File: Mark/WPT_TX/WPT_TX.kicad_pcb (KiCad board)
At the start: 2 copper layers, 113 parts, among them J1 Conn_01x01, J10 Conn_01x01, J2 Conn_01x01, J3 Conn_Coaxial, J4 Conn_Coaxial, J5 Conn_Coaxial, J6 Conn_02x05_Odd_Even, J7 Conn_01x03, J8 Conn_01x04, J9 Conn_01x01, Q1 NMOS, Q2 NMOS, Q3 NMOS, Q4 NMOS, U1 INA240A1D, U10 LM5106, U11 MCP2515-QFN20, U12 MCP2562-E-MF, U13 LM5106, U2 LM2937IMP-3.3, U3 LM2936-5.0, U4 LM2937IMP-12, U5 LMC6032, U6 CD4043BDR, U7 BTS6142DAUMA1, U8 SN74LVC1G14DBV, U9 ATSAMD21G16B-MFT, Y1 32.7680kHz, Y2 8MHz

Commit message: Added input caps
- Forgot input capacitors, oops
- Updated sim based on cap selection, achieving 87% efficiency, low loss on caps!
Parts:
- added C35: 330u, Capacitor_SMD:CP_Elec_10x12.5, F.Cu at (97.1, 56.9)
- added C36: 330u, Capacitor_SMD:CP_Elec_10x12.5, F.Cu at (111.7, 44.9)
- added C37: 330u, Capacitor_SMD:CP_Elec_10x12.5, F.Cu at (111.7, 56.9)
- added C38: 330u, Capacitor_SMD:CP_Elec_10x12.5, F.Cu at (126.2, 44.9)
- moved C10 80.5 mm to (42.7, 80.9)
- moved C11 80.5 mm to (42.7, 85.6)
- moved C13 80.5 mm to (61.4, 69.9)
- moved C16 80.5 mm to (50.4, 80.8)
- moved C17 80.5 mm to (52.6, 72.7)
- moved C18 80.5 mm to (56.5, 72.7)
- moved C19 80.5 mm to (46.6, 85.6)
- moved C2 80.5 mm to (46.6, 80.9)
- moved C20 80.5 mm to (55.8, 77.4)
- moved C22 80.5 mm to (50.4, 83.2)
- moved C23 80.5 mm to (65.3, 69.9)
- moved C24 80.5 mm to (145.8, 85.8)
- moved C25 80.5 mm to (60.3, 74.6)
- moved C30 80.5 mm to (136.0, 95.5)
- moved C31 80.5 mm to (54.3, 80.1)
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
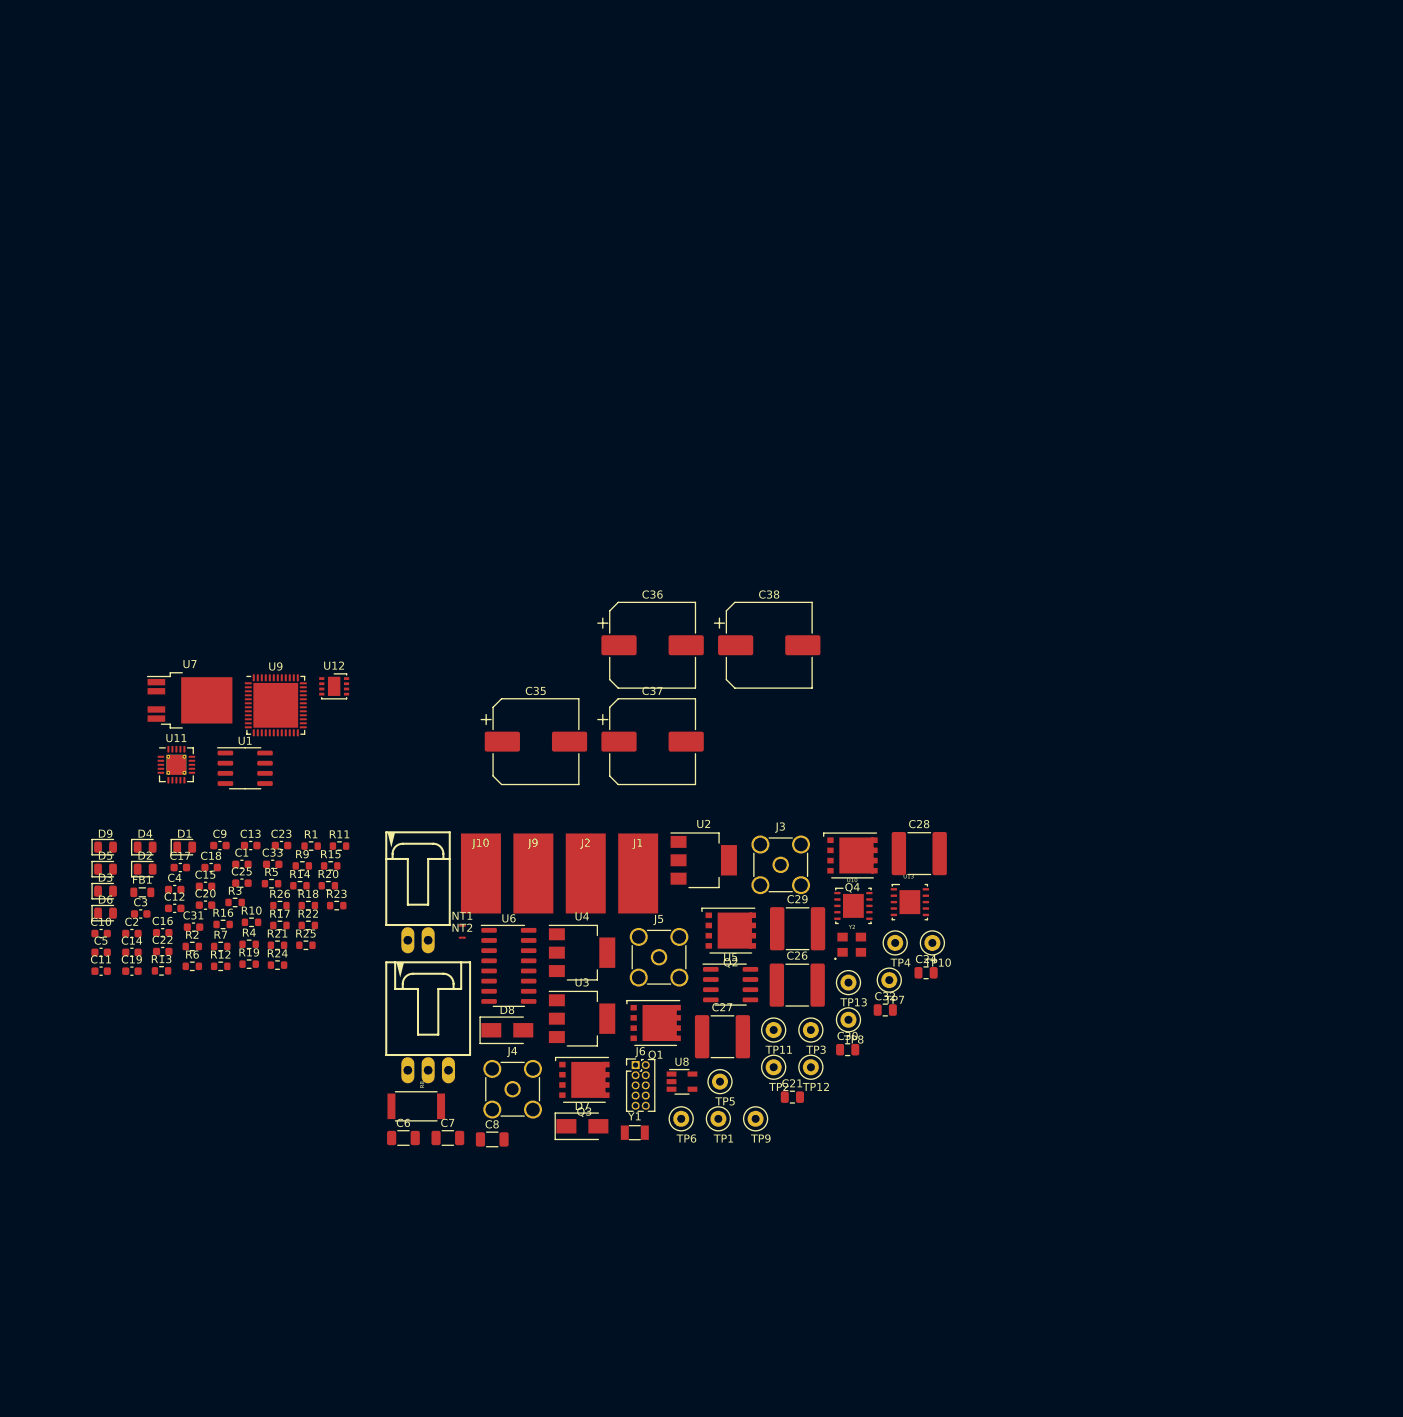
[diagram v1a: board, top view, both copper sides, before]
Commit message: Initial Layout
- Started on layout, board shape.
- Probably will need to get a little larger, but its pretty good
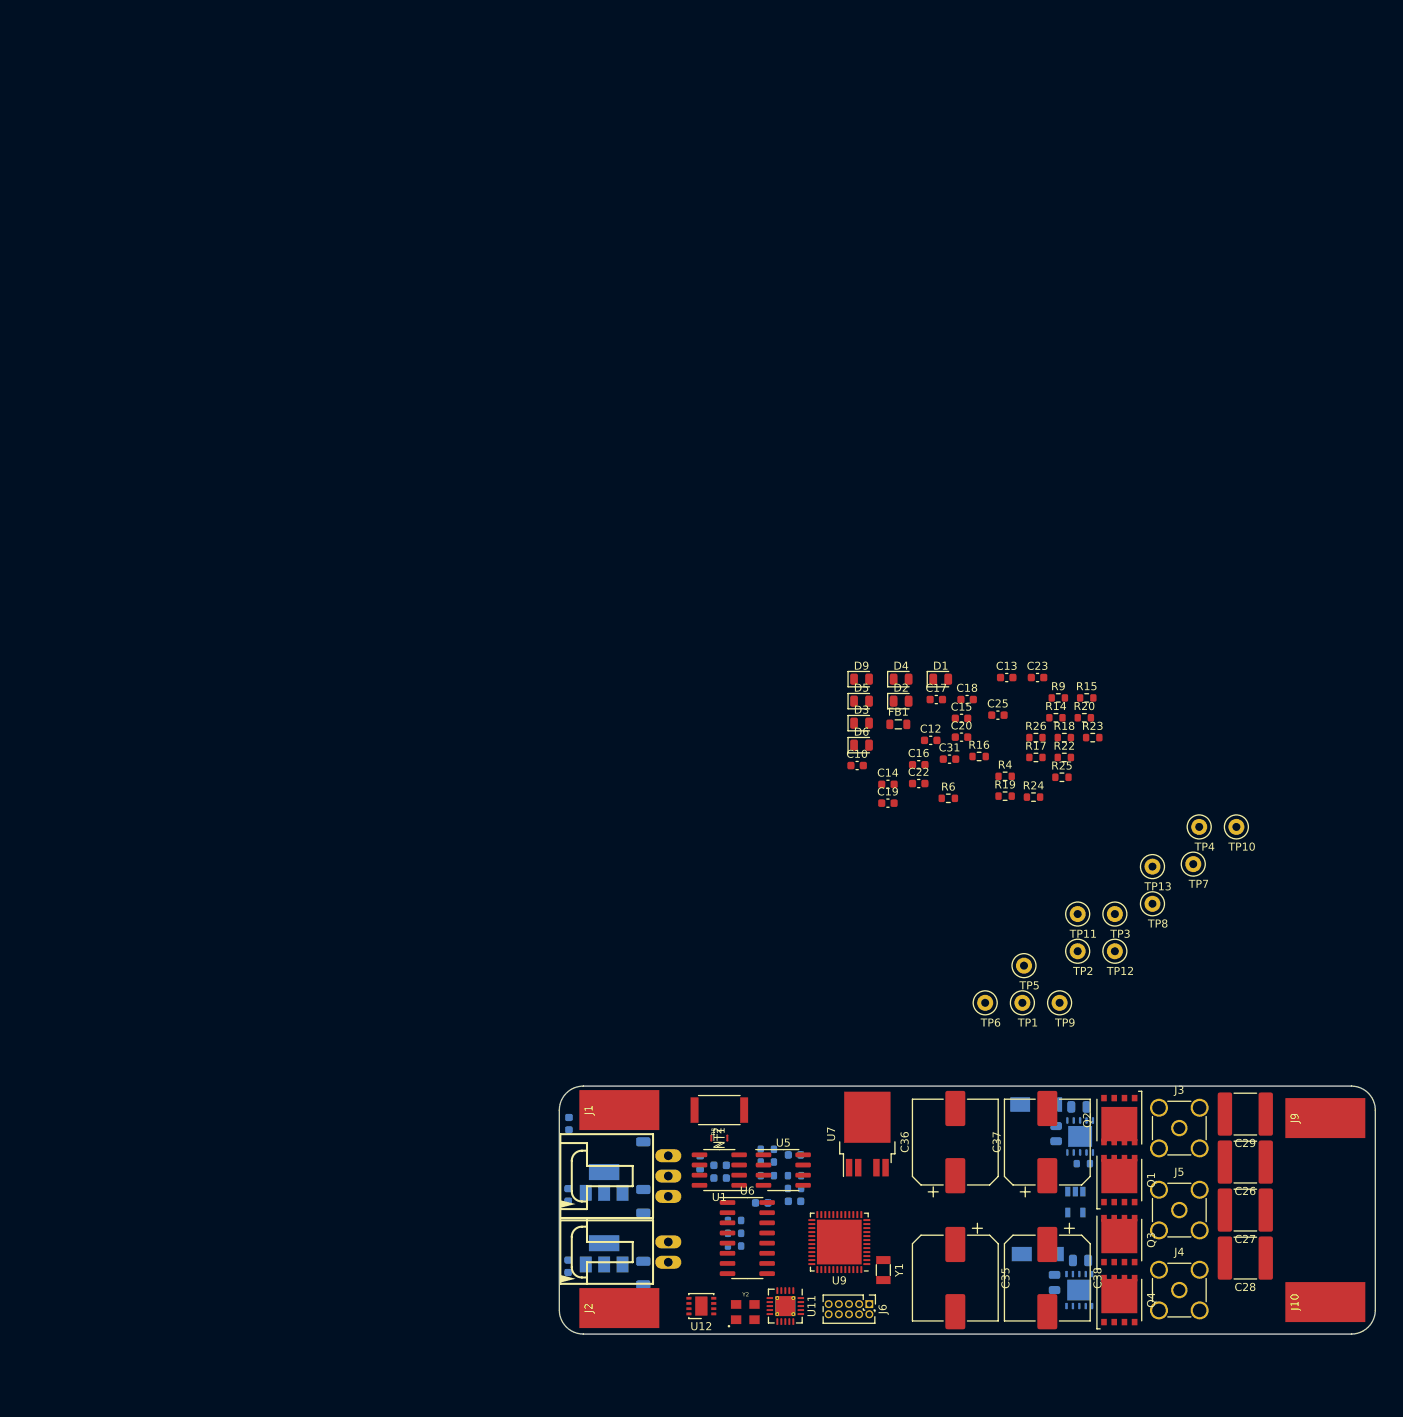
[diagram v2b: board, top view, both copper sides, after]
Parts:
- C1, C11, C2, C21, C24, C3, C30, C32, C33, C4, C5, C6, C7, C8, C9, D7, D8, R1, R10, R11, R12, R13, R2, R21, R3, R5, R7, U10, U13, U2, U3, U4, U8: moved to B.Cu
- moved J10 118.4 mm to (195.8, 127.0), turned to 90 degrees
- moved R21 104.4 mm to (165.5, 109.7)
- moved J9 103.6 mm to (195.8, 104.0), turned to 90 degrees
- moved U11 101.8 mm to (128.2, 127.5), turned to 270 degrees
- moved U7 100.5 mm to (138.5, 106.0), turned to 90 degrees
- moved U9 97.3 mm to (135.0, 119.5), turned to 180 degrees
- moved R15 96.8 mm to (165.9, 51.5)
- moved R23 96.8 mm to (166.7, 56.4)
- moved C10 96.8 mm to (137.2, 59.9)
- moved C12 96.8 mm to (146.4, 56.8)
- moved C13 96.8 mm to (155.9, 48.9)
- moved C15 96.8 mm to (150.3, 54.0)
- moved C16 96.8 mm to (144.9, 59.8)
- moved C17 96.8 mm to (147.1, 51.7)
- moved C18 96.8 mm to (151.0, 51.7)
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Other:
- board outline added: 102 x 31 mm
- copper layers 2 -> 4

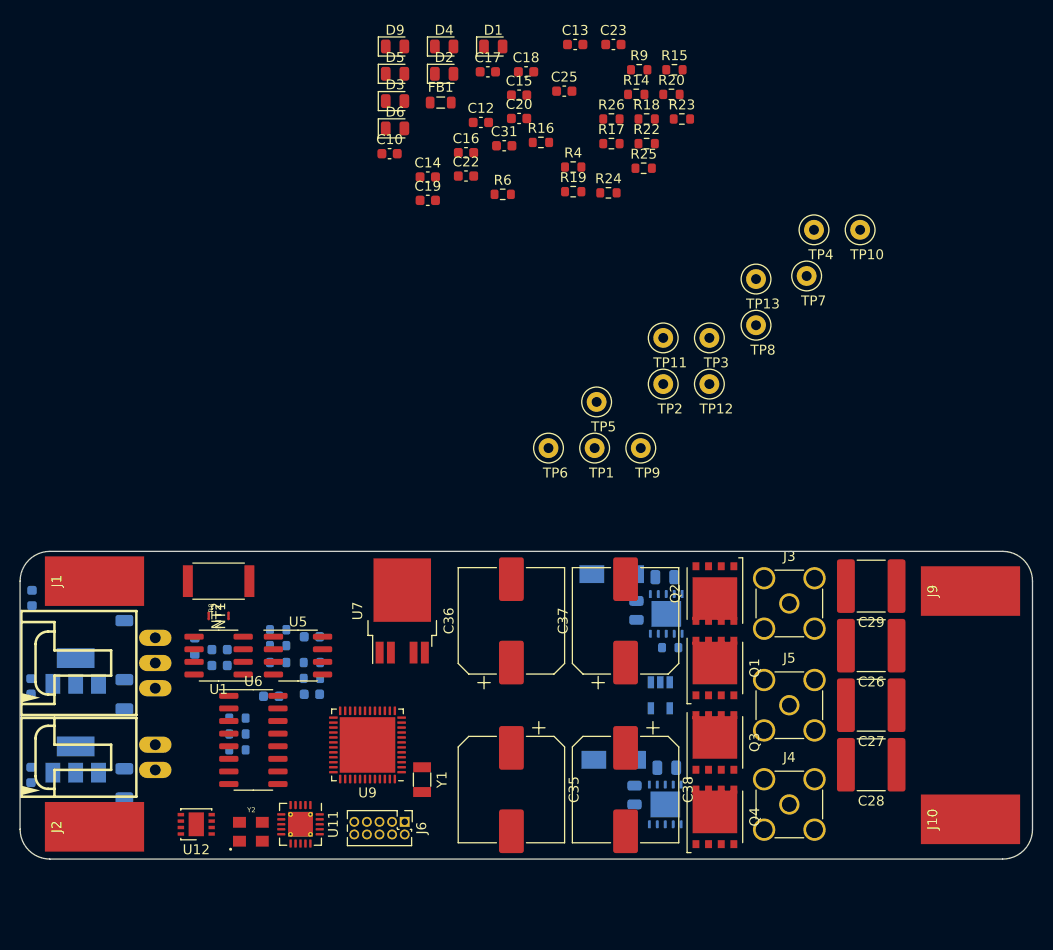
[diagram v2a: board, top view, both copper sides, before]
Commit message: Layout
- Finished expected layout. Going for routing next.
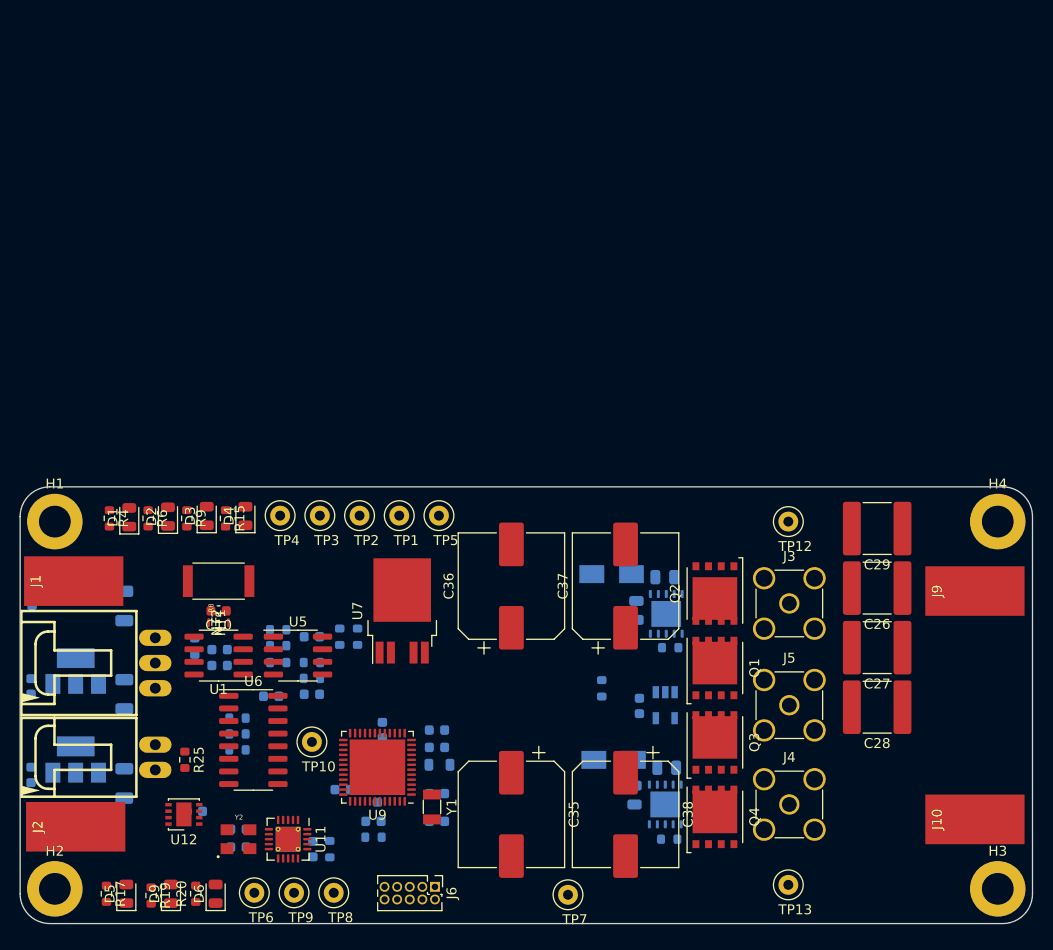
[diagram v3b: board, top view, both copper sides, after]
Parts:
- removed R26: 10k, Resistor_SMD:R_0603_1608Metric
- removed TP11: TestPoint, Testpoints:TestPoint_Loop_D1.80mm_Drill1.0mm_Beaded
- added H1: M3, MountingHole:MountingHole_3.2mm_M3_DIN965_Pad, F.Cu at (103.5, 97.0)
- added H2: M3, MountingHole:MountingHole_3.2mm_M3_DIN965_Pad, F.Cu at (103.5, 134.0)
- added H3: M3, MountingHole:MountingHole_3.2mm_M3_DIN965_Pad, F.Cu at (198.5, 134.0)
- added H4: M3, MountingHole:MountingHole_3.2mm_M3_DIN965_Pad, F.Cu at (198.5, 97.0)
- C12, C13, C14, C15, C16, C17, C18, C19, C20, C22, C23, C25, C31, FB1, R14, R16, R18, R22, R23, R24: moved to B.Cu
- TP1, TP10, TP12, TP13, TP2, TP3, TP4, TP5, TP6, TP7, TP8, TP9: footprint Testpoints:TestPoint_Loop_D1.80mm_Drill1.0mm_Beaded -> TestPoint:TestPoint_Loop_D1.80mm_Drill1.0mm_Beaded
- moved R20 93.7 mm to (117.7, 134.5), turned to 90 degrees
- moved R17 91.1 mm to (108.7, 134.5), turned to 270 degrees
- moved D9 88.3 mm to (115.2, 134.5), turned to 90 degrees
- moved C23 87.6 mm to (122.0, 128.0), turned to 180 degrees
- moved D5 86.9 mm to (110.7, 134.5), turned to 90 degrees
- moved R19 82.7 mm to (113.2, 134.7), turned to 270 degrees
- moved R23 81.7 mm to (131.2, 130.0), turned to 90 degrees
- moved C25 80.5 mm to (129.5, 130.0), turned to 270 degrees
- moved D6 79.2 mm to (119.7, 134.5), turned to 90 degrees
- moved R18 77.4 mm to (135.6, 128.8), turned to 180 degrees
- moved C13 76.7 mm to (142.0, 124.4)
- moved C17 76.4 mm to (135.6, 127.2)
- moved TP10 75.6 mm to (129.4, 119.2)
- moved R25 75.4 mm to (116.6, 121.0), turned to 270 degrees
- moved C31 74.0 mm to (117.6, 126.2), turned to 180 degrees
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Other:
- board size 102 x 31 mm -> 102 x 44 mm

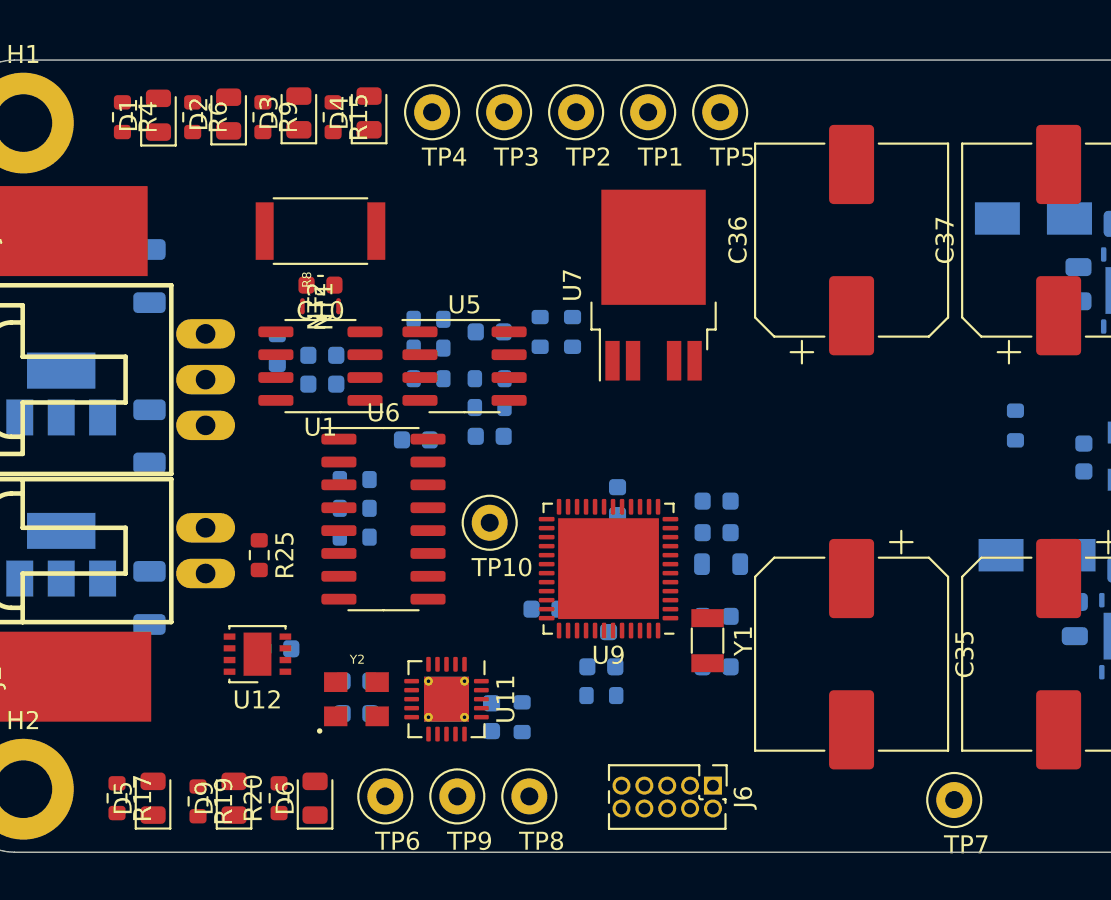
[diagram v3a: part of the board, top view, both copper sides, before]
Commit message: Some Routing
- Most non-plane routing is complete
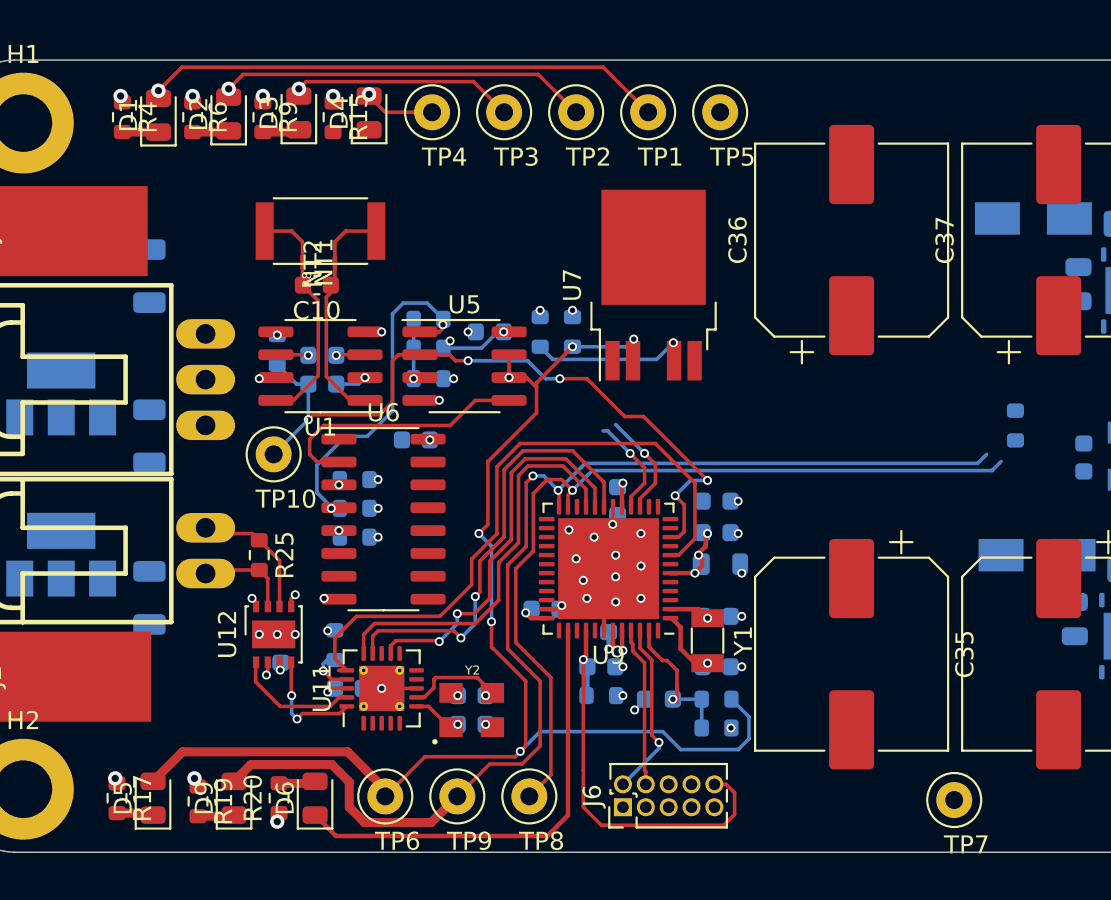
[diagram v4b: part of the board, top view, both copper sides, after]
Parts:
- moved R11 21.8 mm to (142.0, 129.0)
- moved R12 21.8 mm to (142.0, 130.6)
- moved C33 17.4 mm to (138.8, 129.0), turned to 180 degrees
- moved TP10 12.6 mm to (117.4, 115.4)
- moved R23 11.1 mm to (120.8, 126.0), turned to 270 degrees
- moved C25 8.08 mm to (121.6, 128.4), turned to 0 degrees
- moved C23 6.45 mm to (128.4, 128.8)
- moved C22 6.43 mm to (128.4, 130.4)
- moved Y2 6.43 mm to (128.4, 129.6)
- moved J6 5.14 mm to (136.8, 135.0), turned to 90 degrees
- moved U11 3.65 mm to (123.4, 128.4), turned to 90 degrees
- moved NT1 2.45 mm to (119.0, 104.7)
- moved NT2 2.38 mm to (120.8, 104.8)
- moved U12 1.42 mm to (117.4, 125.4), turned to 90 degrees
- moved C10 0.20 mm to (119.8, 106.0)
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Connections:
- U11 pad 15: /SPI0_MOSI -> /SPI0_MISO
- U9 pad 21: /SPI0_MOSI -> /SPI0_MISO
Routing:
- net /FAULT_OL: track 0.00 -> 73.7 mm, vias 0 -> 6
- net /HBridge_EN: track 0.00 -> 64.9 mm, vias 0 -> 2
- net /HBridge_PWM: track 0.00 -> 46.8 mm, vias 0 -> 1
- net /ISEN: track 0.00 -> 40.0 mm, vias 0 -> 5
- net +3V3: track 0.00 -> 38.0 mm, vias 0 -> 10
- net /SPI0_CS: track 0.00 -> 35.8 mm
- net GND: track 0.00 -> 31.7 mm, vias 0 -> 46
- net +5V: track 0.00 -> 28.9 mm, vias 0 -> 7
- net Net-(D6-Pad1): track 0.00 -> 25.3 mm
- net /SPI0_MOSI: track 0.00 -> 24.6 mm, vias 0 -> 2
- net /~RST~: track 0.00 -> 23.6 mm, vias 0 -> 1
- net /SPI0_MISO: track 0.00 -> 22.2 mm
- net /SPI0_SCLK: track 0.00 -> 21.5 mm, vias 0 -> 2
- net Net-(R5-Pad2): track 0.00 -> 20.2 mm, vias 0 -> 2
- net /FAULT_OL_SR: track 0.00 -> 14.6 mm
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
